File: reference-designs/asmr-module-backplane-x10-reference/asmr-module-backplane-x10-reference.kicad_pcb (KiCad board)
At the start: 2 copper layers, 385 x 67.5 mm, 45 parts, among them J1 PCI-64P, J10 PCI-64P, J2 PCI-64P, J3 PCI-64P, J4 PCI-64P, J5 PCI-64P, J6 PCI-64P, J7 PCI-64P, J8 PCI-64P, J9 PCI-64P

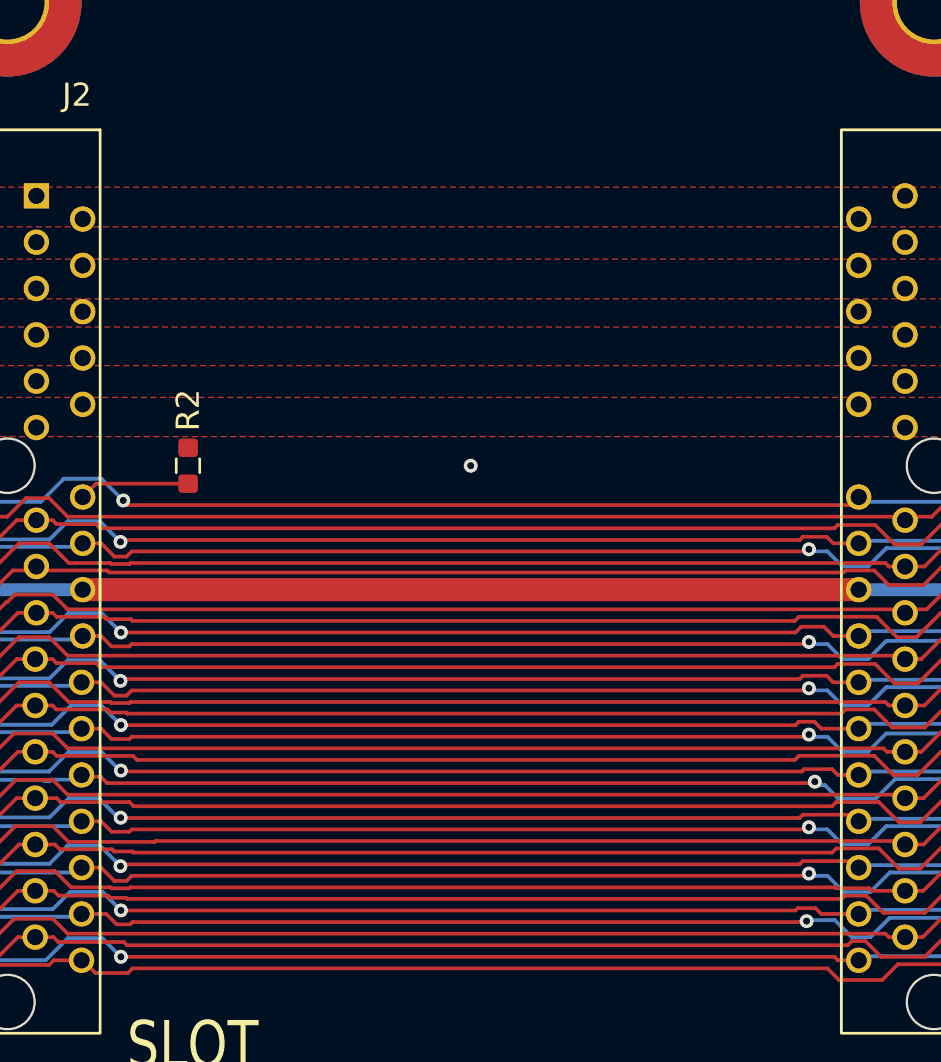
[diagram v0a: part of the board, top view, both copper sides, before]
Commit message: Gerber settings and more PCB silk changes.
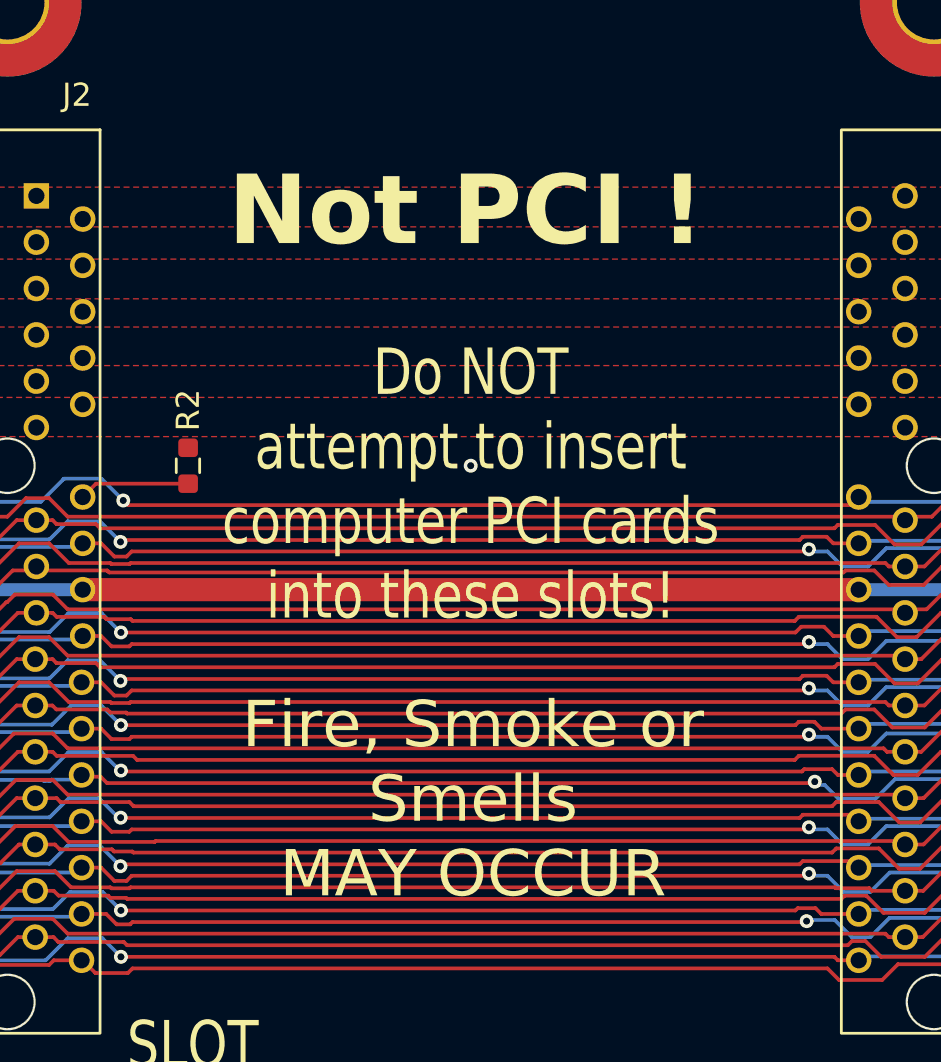
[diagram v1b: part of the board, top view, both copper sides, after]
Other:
- board text added: "Do NOT attempt to insert computer PCI cards into these slots!"
- board text added: "Fire, Smoke or Smells MAY OCCUR"
- board text added: "Not PCI !"
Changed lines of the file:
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@@
 			(plot_on_all_layers_selection 0x00000000_00000000_00000000_00000000)
 			(disableapertmacros no)
-			(usegerberextensions no)
+			(usegerberextensions yes)
 			(usegerberattributes yes)
 			(usegerberadvancedattributes yes)
@@
 			(outputformat 1)
 			(mirror no)
-			(drillshape 1)
+			(drillshape 0)
 			(scaleselection 1)
-			(outputdirectory "")
+			(outputdirectory "gerber/")
 		)
 	)
@@
 		)
 	)
+	(gr_text "Not PCI !"
+		(at 189.8 139 0)
+		(layer "F.SilkS")
+		(effects
+			(font
+				(size 3 3)
+				(thickness 0.6)
+				(bold yes)
+			)
+		)
+	)
 	(gr_text "1"
 		(at 138.1 180 0)
@@
 		)
 	)
+	(gr_text "Fire, Smoke or\nSmells\nMAY OCCUR"
+		(at 190.1 164.4 0)
+		(layer "F.SilkS")
+		(effects
+			(font
+				(size 2 2)
+				(thickness 0.3)
+			)
+		)
+	)
 	(gr_text "9"
 		(at 458 180 0)
@@
 			)
 		)
+	)
+	(gr_text "Do NOT\nattempt to insert\ncomputer PCI cards \ninto these slots!"
+		(at 190 150.8 0)
+		(layer "F.SilkS")
+		(effects
+			(font
+				(size 2 1.6)
+				(thickness 0.3)
+			)
+		)
